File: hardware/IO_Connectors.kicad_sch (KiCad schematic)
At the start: 20 parts, among them J3 USB_B_Micro

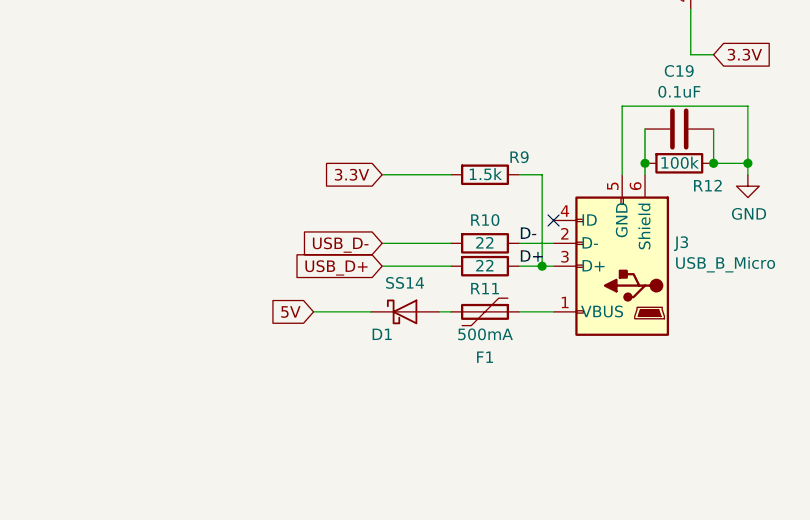
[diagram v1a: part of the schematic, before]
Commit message: Update the 1N4148 diodes to B5819W. The 1N was too puny to serve as protection.
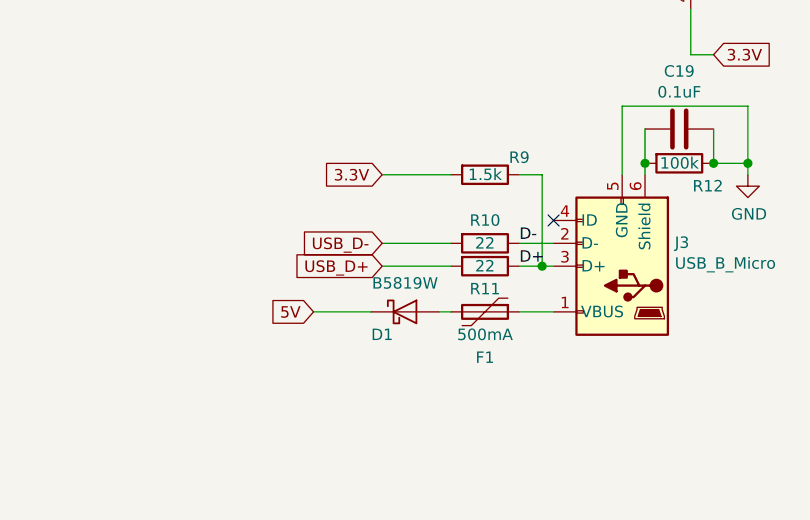
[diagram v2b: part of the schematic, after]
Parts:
- D1: value SS14 -> B5819W; footprint Diode_SMD:D_SMA -> Diode_SMD:D_SOD-123; LCSC Part # C2480 -> C8598; Part # SS14 -> B5819W

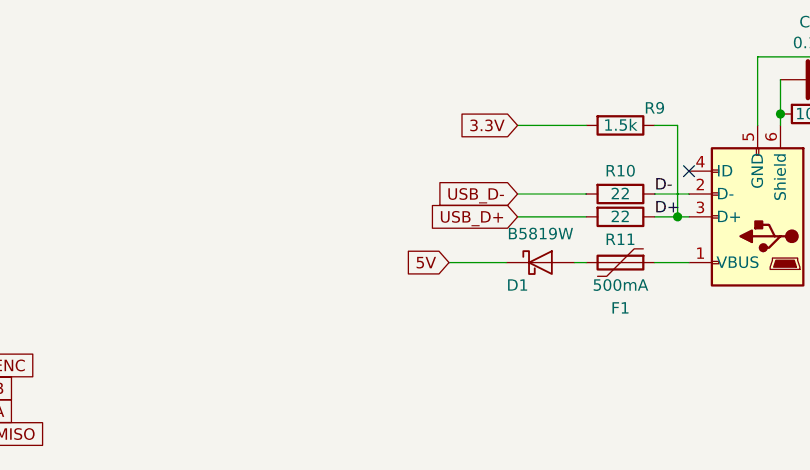
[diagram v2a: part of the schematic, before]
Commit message: Update to rev 5. Add jumper to select USB powering the board or not.
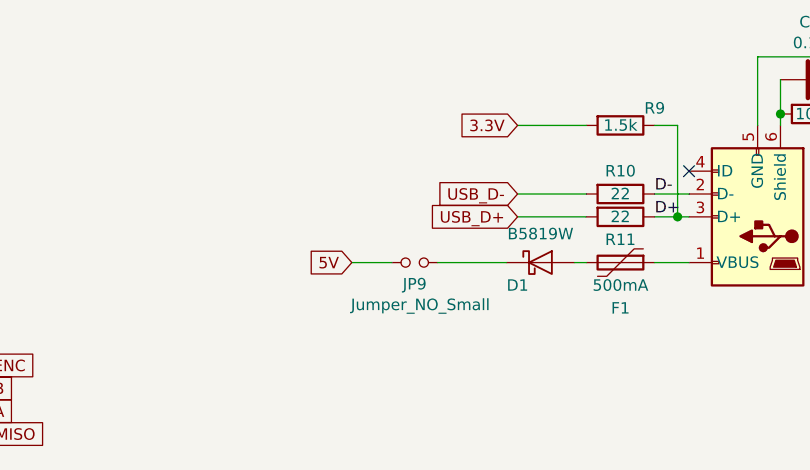
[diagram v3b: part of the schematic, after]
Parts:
- added JP9: Jumper_NO_Small, Connector_PinHeader_2.54mm:PinHeader_1x02_P2.54mm_Vertical, symbol Device:Jumper_NO_Small
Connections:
- net 5V: now also JP9.1; no longer D1.1 (K)
- new net: D1.1 (K), JP9.2
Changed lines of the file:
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@@
+    (stroke (width 0) (type solid) (color 0 0 0 0))
+  )
+  (wire (pts (xy 171.45 115.57) (xy 175.895 115.57))
     (stroke (width 0) (type solid) (color 0 0 0 0))
   )
@@
     (stroke (width 0) (type solid) (color 0 0 0 0))
   )
-  (wire (pts (xy 188.595 115.57) (xy 182.245 115.57))
+  (wire (pts (xy 180.975 115.57) (xy 188.595 115.57))
     (stroke (width 0) (type solid) (color 0 0 0 0))
   )
@@
     (effects (font (size 1.27 1.27)) (justify right))
   )
-  (global_label "5V" (shape input) (at 182.245 115.57 180)    (property "Intersheet References" "${INTERSHEET_REFS}" (id 0) (at 0 0 0)
+  (global_label "5V" (shape input) (at 171.45 115.57 180)    (property "Intersheet References" "${INTERSHEET_REFS}" (id 0) (at -10.795 0 0)
       (effects (font (size 1.27 1.27)) hide)
     )
@@
     (effects (font (size 1.27 1.27)) (justify left))
   )
+  (symbol (lib_id "Device:Jumper_NO_Small") (at 178.435 115.57 0) (unit 1)
+    (in_bom no) (on_board yes)
+    (property "Reference" "JP9" (id 0) (at 178.435 117.9638 0))
+    (property "Value" "Jumper_NO_Small" (id 1) (at 179.07 120.2625 0))
+    (property "Footprint" "Connector_PinHeader_2.54mm:PinHeader_1x02_P2.54mm_Vertical" (id 2) (at 178.435 115.57 0)
+      (effects (font (size 1.27 1.27)) hide)
+    )
+    (property "Datasheet" "~" (id 3) (at 178.435 115.57 0)
+      (effects (font (size 1.27 1.27)) hide)
+    )
+  )
   (symbol (lib_id "power:GND") (at 58.42 65.405 0) (unit 1)

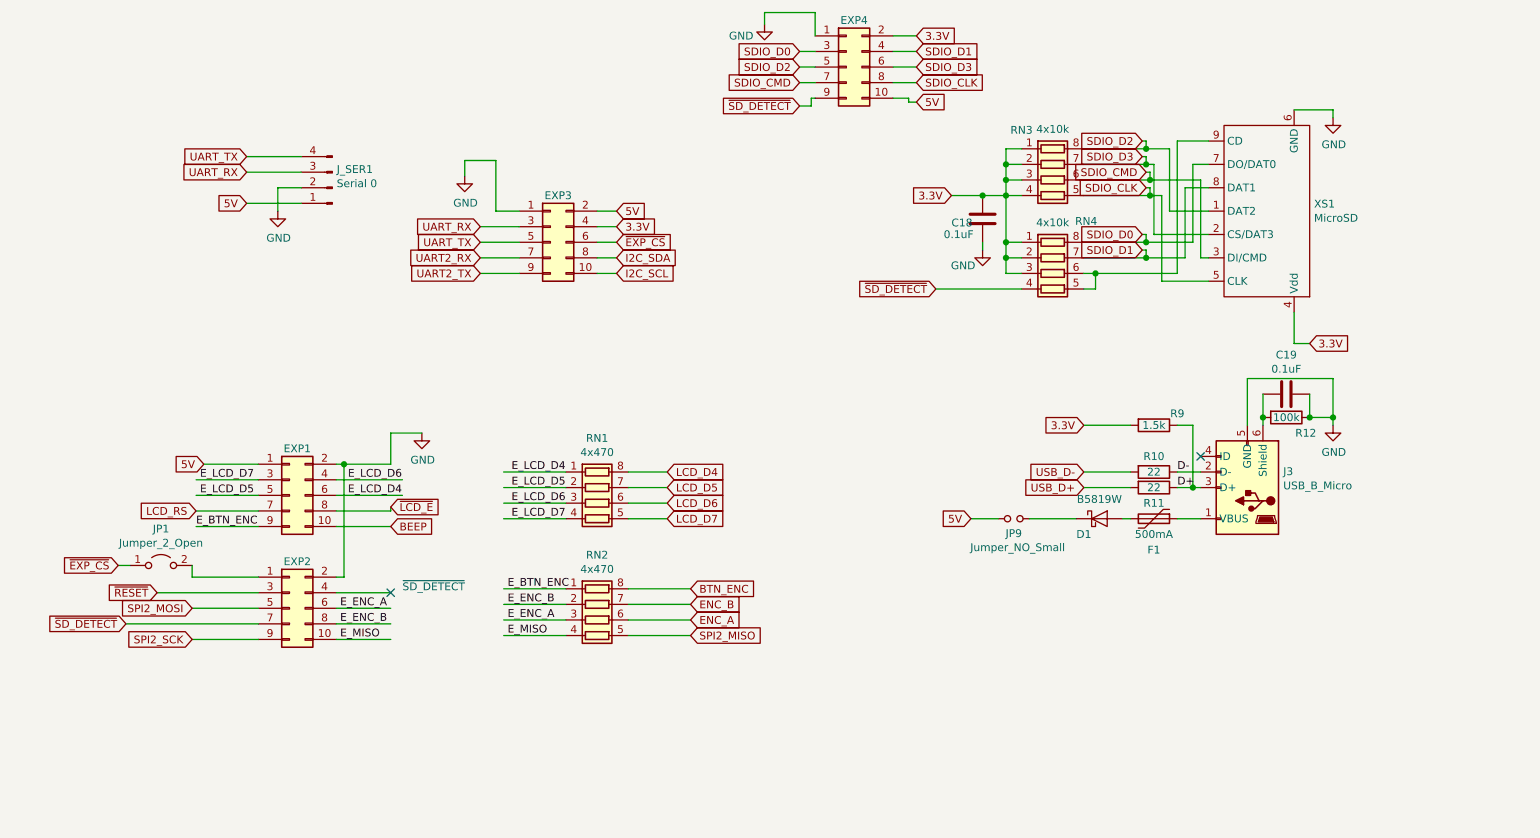
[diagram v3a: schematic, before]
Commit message: Added CAN
- Added CAN interface (PD0-1) with RJ 6p6c terminal
- SD card moved to back /left side and switched to SPI mode
- removed  EXP4 headrr
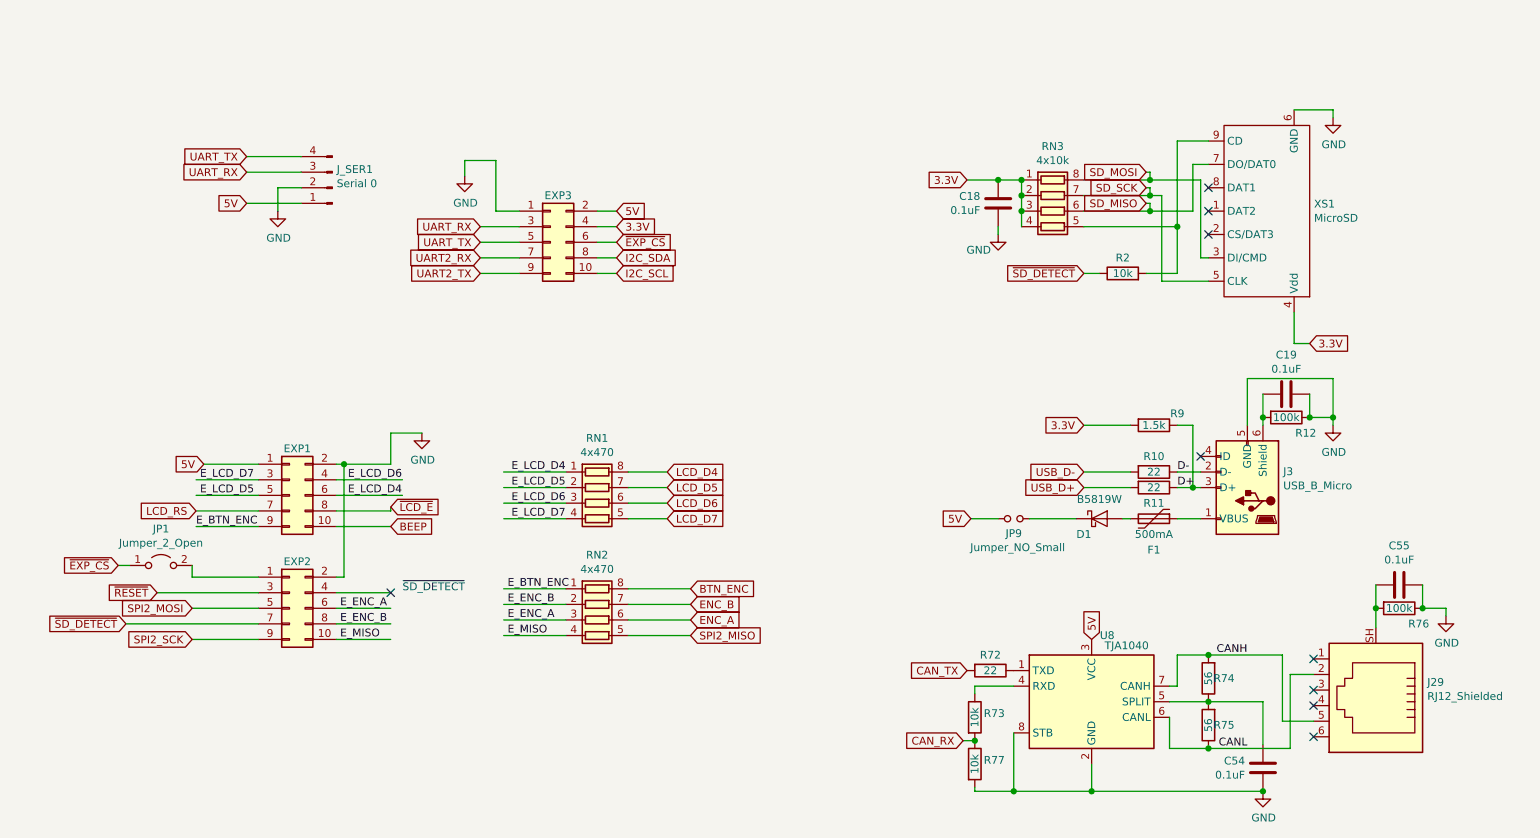
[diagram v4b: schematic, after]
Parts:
- removed EXP4: IDC 2x5, Connector_IDC:IDC-Header_2x05_P2.54mm_Vertical, symbol Connector_Generic:Conn_02x05_Odd_Even
- removed RN4: 4x10k, Resistor_SMD:R_Array_Convex_4x0603, symbol Device:R_Pack04
- added C54, C55: 0.1uF, PrntrBoardV2:C_0603_1608Metric, symbol Device:C
- added J29: RJ12_Shielded, Connector_RJ:RJ12_Amphenol_54601, symbol Connector:RJ12_Shielded
- added R2, R73, R77: 10k, PrntrBoardV2:R_0603_1608Metric, symbol Device:R
- added R72: 22, PrntrBoardV2:R_0603_1608Metric, symbol Device:R
- added R74, R75: 56, PrntrBoardV2:R_0603_1608Metric, symbol Device:R
- added R76: 100k, PrntrBoardV2:R_0603_1608Metric, symbol Device:R
- added U8: TJA1040, Package_SO:SOIC-8_3.9x4.9mm_P1.27mm, symbol Interface_CAN_LIN:TJA1042T
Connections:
- net SDIO_D0 is gone; now on net SD_MISO: XS1.7 (DO/DAT0)
- net 5V: now also U8.3 (VCC)
- net GND: now also C54.1, C55.1, R76.1, R77.2, U8.2 (GND), U8.8 (STB)
- net ~SD_DETECT: now also R2.1
- net at XS1.9 (CD): now also RN3.5 (R4.2), R2.2
- net SDIO_CLK renamed SD_SCK
- net SD_SCK: now also RN3.7 (R2.2); no longer RN3.5 (R4.2)
- net SDIO_CMD renamed SD_MISO
- net SD_MISO: no longer XS1.3 (DI/CMD)
- net SDIO_D1: no longer names the net of XS1.8 (DAT1)
- net SDIO_D2: no longer names the net of XS1.1 (DAT2)
- net SDIO_D2: no longer RN3.8 (R1.2)
- net SDIO_D3: no longer names the net of XS1.2 (CS/DAT3)
- net SDIO_D3: no longer RN3.7 (R2.2)
- new net: C54.2, R74.1, R75.2, U8.5 (SPLIT)
- new net: R72.1, U8.1 (TXD)
- new net: C55.2, J29.SH, R76.2
- new net: R73.1, U8.4 (RXD)
- new net CANH: J29.5, R74.2, U8.7 (CANH)
- new net CANL: J29.2, R75.1, U8.6 (CANL)
- new net CAN_RX: R73.2, R77.1
- new net CAN_TX: R72.2
- new net SD_MOSI: RN3.8 (R1.2), XS1.3 (DI/CMD)
- no-connect marks 2 -> 9
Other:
- moved on the sheet: C18, RN3
